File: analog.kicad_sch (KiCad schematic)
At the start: 51 parts, among them J10 Sensor harness, U9 ADS1115

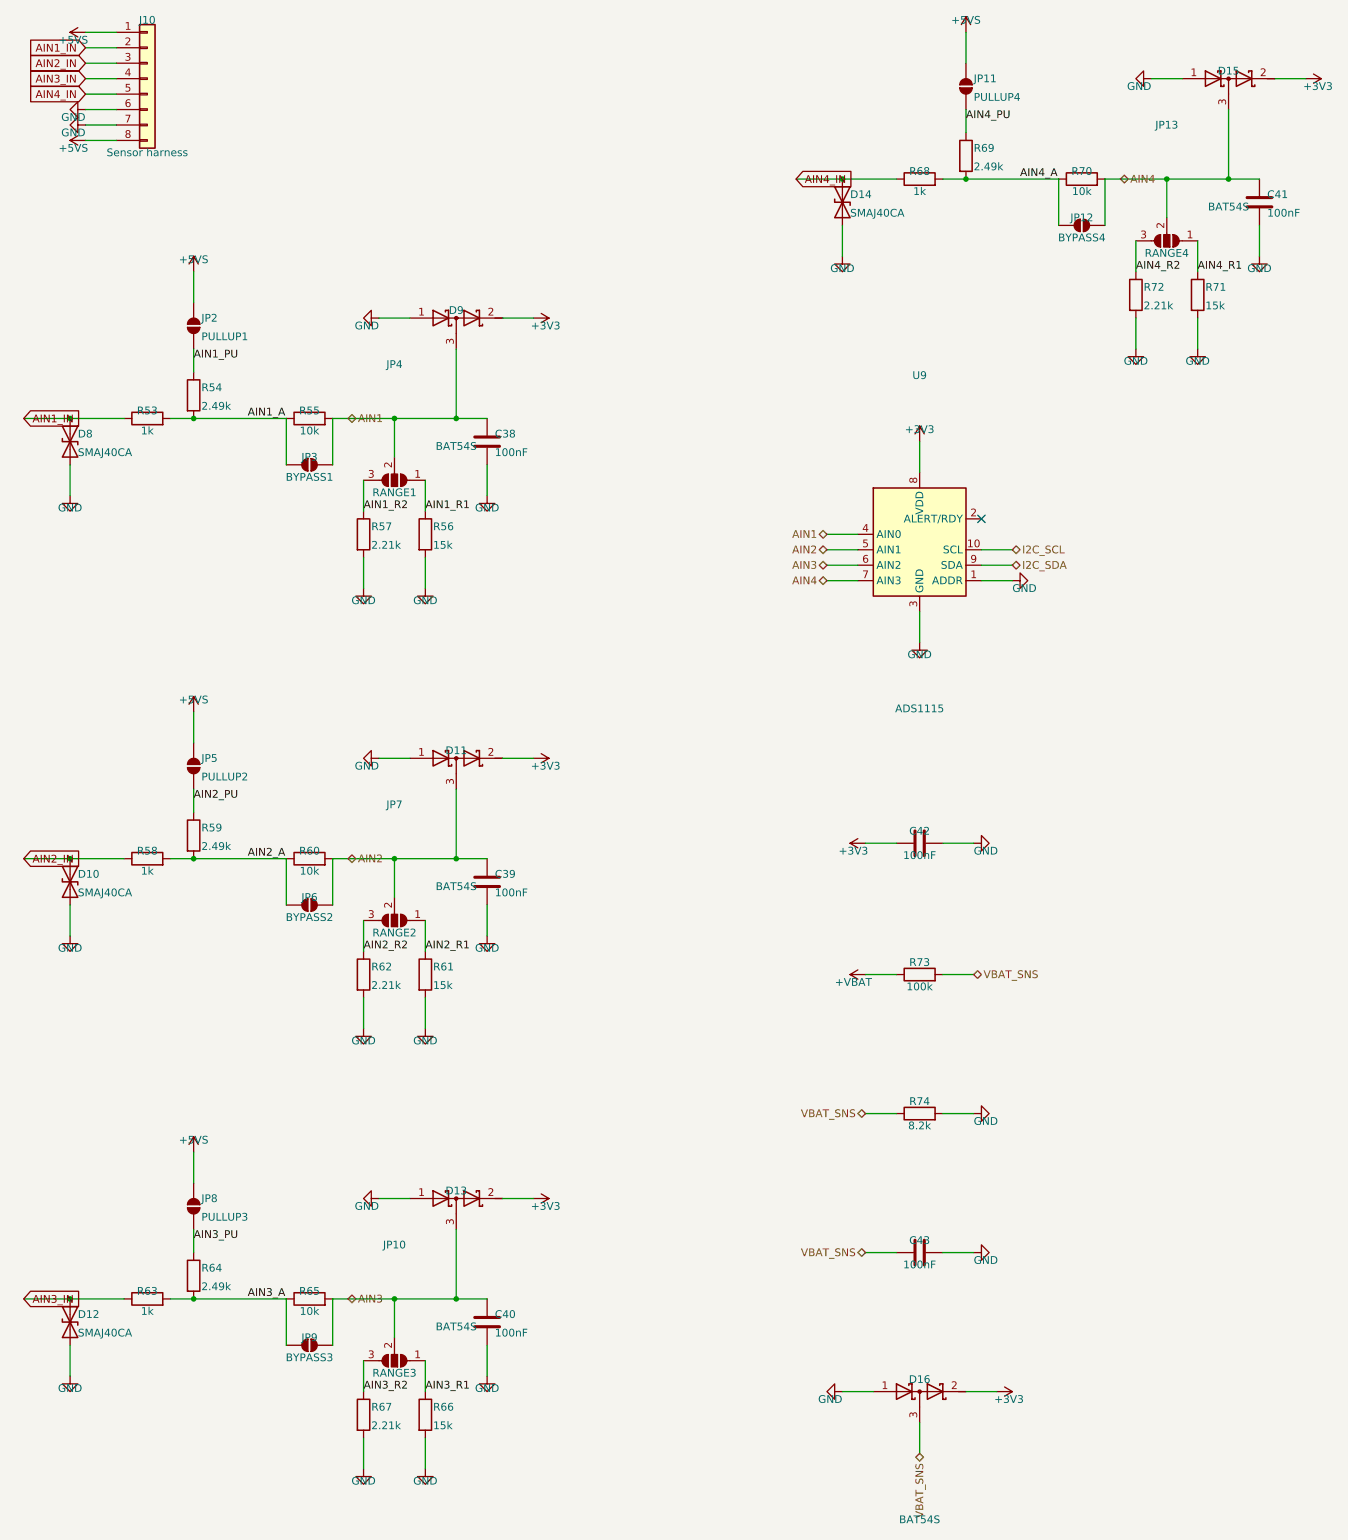
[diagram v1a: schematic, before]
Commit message: USB OVP, card-slot ESD, SD test points, and a gold-standard schematic
Hardware, all simulation- or review-driven:
- USB overvoltage cutoff: TLV431 + AO3401 + MMBT3906 series switch on
  VBUS, tripping at 5.77 V. Re-simulated: a compliant 5 V source passes
  at 4.99 V, the switch opens at 5.95 V of brick, and the +5V rail never
  exceeds 5.2 V from anything up to 14 V -- where a 9 V brick previously
  drove it to 8.4 V against the TJA1051's 6 V absolute maximum.
  Off-the-shelf OVP parts were rejected first: the TPS25200 class cuts
  off near 7 V, which is no protection for a 6 V limit.
- Two SRV05-4 arrays clamp every microSD card contact (LCSC C13612);
  until now the ESP32's ~2 kV pin diodes were all that stood behind a
  card swapped by hand after every session.
- A second USBLC6 clamps the USB-C CC pins -- the first contacts every
  plug insertion touches, previously landing on bare 5.1k resistors.
- Test points on SD_CLK and SD_CMD, the most likely scope targets at
  bring-up and otherwise reachable only on fine-pitch pads.

The schematic itself was rebuilt to read like a reference design
(RejsaCAN was the benchmark): every circuit is now a hand-drawn block --
power-fail detector, sensor-rail switch, USB OVP, connector pull-
resistor clusters, and a single utility panel for test points, ERC
flags, mounting holes and the power LED. Sentence-length values became
part numbers ("0.2A PTC", "AO3401A", "600R") with ratings kept in
hidden fields, which also answers the external review's value-hygiene
findings. Title blocks carry rev B and a date. The Power sheet shrank
from A2 back to A3 in the process.

gen/README.md now documents the whole pipeline -- stages, the block-
drawing conventions with per-rotation pin geometry, the junction rules,
and the traps (property newlines, off-grid points, anchors keeping
their natural rotation) -- so the next board reuses all of it.

Board: 84 x 100, 0 DRC violations, 0 unconnected, 0 courtyard overlaps,
physical audit clean. BOM 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
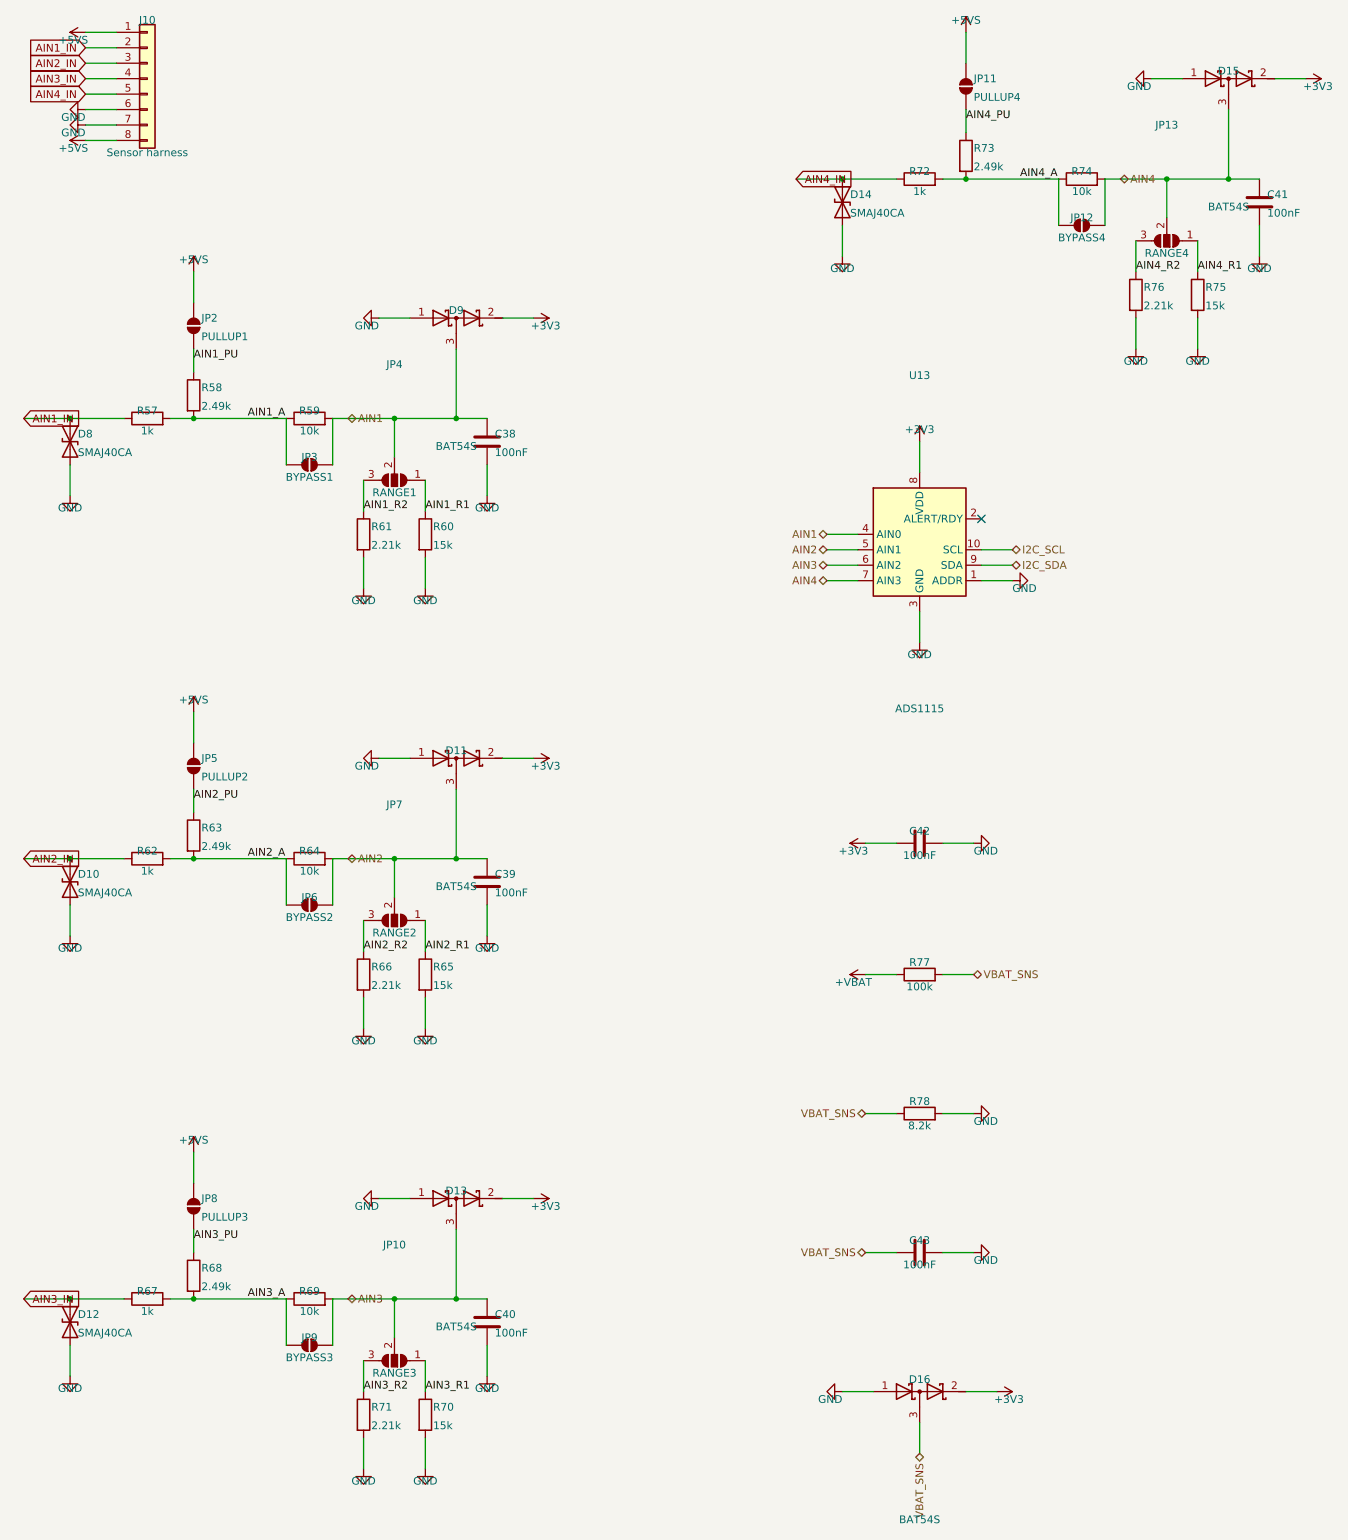
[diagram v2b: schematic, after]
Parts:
- removed R53: 1k, Resistor_SMD:R_0805_2012Metric, symbol Device:R
- removed R54: 2.49k, Resistor_SMD:R_0805_2012Metric, symbol Device:R
- removed R55: 10k, Resistor_SMD:R_0805_2012Metric, symbol Device:R
- removed R56: 15k, Resistor_SMD:R_0805_2012Metric, symbol Device:R
- removed U9: ADS1115, Package_SO:VSSOP-10_3x3mm_P0.5mm, symbol Analog_ADC:ADS1115IDGS
- added R75: 15k, Resistor_SMD:R_0805_2012Metric, symbol Device:R
- added R76: 2.21k, Resistor_SMD:R_0805_2012Metric, symbol Device:R
- added R77: 100k, Resistor_SMD:R_0805_2012Metric, symbol Device:R
- added R78: 8.2k, Resistor_SMD:R_0805_2012Metric, symbol Device:R
- added U13: ADS1115, Package_SO:VSSOP-10_3x3mm_P0.5mm, symbol Analog_ADC:ADS1115IDGS
- R57: value 2.21k -> 1k; Note 0-16V range: 16.0V in -> ~2.67V at the ADC (1k series inclu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 -> Ch1 series/fault-current limit; 0.1% thin film -- it is ins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
- R58: value 1k -> 2.49k; Note Ch2 series/fault-current limit; 0.1% thin film -- it is ins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 -> Ch1 bias resistor; Tolerance 0.1% -> (none)
- R59: value 2.49k -> 10k; Note Ch2 bias resistor -> Ch1 divider upper leg, 0.1% thin film for AFR-grade accuracy; Tolerance (none) -> 0.1%
- R60: value 10k -> 15k; Note Ch2 divider upper leg, 0.1% thin film for AFR-grade accuracy -> 0-5V range: 5.0V in -> ~2.88V at the ADC (1k series include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
- R61, R66, R71: value 15k -> 2.21k; Note 0-5V range: 5.0V in -> ~2.88V at the ADC (1k series include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 -> 0-16V range: 16.0V in -> ~2.67V at the ADC (1k series inclu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
- R62: value 2.21k -> 1k; Note 0-16V range: 16.0V in -> ~2.67V at the ADC (1k series inclu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 -> Ch2 series/fault-current limit; 0.1% thin film -- it is ins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
- R63: value 1k -> 2.49k; Note Ch3 series/fault-current limit; 0.1% thin film -- it is ins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 -> Ch2 bias resistor; Tolerance 0.1% -> (none)
- R64: value 2.49k -> 10k; Note Ch3 bias resistor -> Ch2 divider upper leg, 0.1% thin film for AFR-grade accuracy; Tolerance (none) -> 0.1%
- R65: value 10k -> 15k; Note Ch3 divider upper leg, 0.1% thin film for AFR-grade accuracy -> 0-5V range: 5.0V in -> ~2.88V at the ADC (1k series include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
- R67: value 2.21k -> 1k; Note 0-16V range: 16.0V in -> ~2.67V at the ADC (1k series inclu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 -> Ch3 series/fault-current limit; 0.1% thin film -- it is ins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
- R68: value 1k -> 2.49k; Note Ch4 series/fault-current limit; 0.1% thin film -- it is ins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 -> Ch3 bias resistor; Tolerance 0.1% -> (none)
- R69: value 2.49k -> 10k; Note Ch4 bias resistor -> Ch3 divider upper leg, 0.1% thin film for AFR-grade accuracy; Tolerance (none) -> 0.1%
- R70: value 10k -> 15k; Note Ch4 divider upper leg, 0.1% thin film for AFR-grade accuracy -> 0-5V range: 5.0V in -> ~2.88V at the ADC (1k series include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
- R72: value 2.21k -> 1k; Note 0-16V range: 16.0V in -> ~2.67V at the ADC (1k series inclu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 -> Ch4 series/fault-current limit; 0.1% thin film -- it is ins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
- R73: value 100k -> 2.49k; Note Battery monitor: divide by 11 -> Ch4 bias resistor
- R74: value 8.2k -> 10k; Note Divide by 13.2, not 11: at 36V the 11:1 divider put 3.27V o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 -> Ch4 divider upper leg, 0.1% thin film for AFR-grade accuracy; Tolerance (none) -> 0.1%
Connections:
- net +3V3: now also U13.8 (VDD)
- net +VBAT: now also R77.1; no longer R73.1
- net AIN1: now also R59.2, U13.4 (AIN0)
- net AIN1_A: now also R57.2, R58.2, R59.1
- net AIN1_IN: now also R57.1
- net AIN1_PU: now also R58.1
- net AIN1_R1: now also R60.1
- net AIN1_R2: now also R61.1; no longer R57.1
- net AIN2: now also R64.2, U13.5 (AIN1); no longer R60.2
- net AIN2_A: now also R62.2, R63.2, R64.1; no longer R58.2, R59.2, R60.1
- net AIN2_IN: now also R62.1; no longer R58.1
- net AIN2_PU: now also R63.1; no longer R59.1
- net AIN2_R1: now also R65.1; no longer R61.1
- net AIN2_R2: now also R66.1; no longer R62.1
- net AIN3: now also R69.2, U13.6 (AIN2); no longer R65.2
- net AIN3_A: now also R67.2, R68.2, R69.1; no longer R63.2, R64.2, R65.1
- net AIN3_IN: now also R67.1; no longer R63.1
- net AIN3_PU: now also R68.1; no longer R64.1
- net AIN3_R1: now also R70.1; no longer R66.1
- net AIN3_R2: now also R71.1; no longer R67.1
- net AIN4: now also R74.2, U13.7 (AIN3); no longer R70.2
- net AIN4_A: now also R72.2, R73.2, R74.1; no longer R68.2, R69.2, R70.1
- net AIN4_IN: now also R72.1; no longer R68.1
- net AIN4_PU: now also R73.1; no longer R69.1
- net AIN4_R1: now also R75.1; no longer R71.1
- net AIN4_R2: now also R76.1; no longer R72.1
- net GND: now also R60.2, R65.2, R70.2, R75.2, R76.2, R78.2, U13.1 (ADDR), U13.3 (GND); no longer R57.2, R62.2, R67.2, R72.2, R74.2
- net I2C_SCL: now also U13.10 (SCL)
- net I2C_SDA: now also U13.9 (SDA)
- net VBAT_SNS: now also R77.2, R78.1; no longer R73.2, R74.1
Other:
- moved on the sheet: R57, R58, R59, R60, R61, R62, R63, R64, R65, R66, R67, R68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

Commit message: Studies 9-11, post-route extraction, strap audit, readable labels, production BOM numbers
New tests, run against the final board:
- audit_routes.py: Dijkstra IR drop over the routed copper (worst 55 mV
  at rated current), SD/USB/CAN routed lengths (USB pair matched to
  1.1 mm), buck switch-node copper area. All clean.
- audit_straps.py: every ESP32-S3 strapping pin against what the netlist
  hangs on it; all five boot in their required state.
- simulate.py 9, stability: the LM5164 ripple-injection criterion across
  the input window. Found the ramp thin (10.6 mV) at a legitimate 8 V
  operating point -- ramp caps changed 3.3 nF -> 2.2 nF, now 15.8 mV+
  everywhere above crank voltages. Board rebuilt: 0 DRC, 0 unconnected,
  0 overlaps.
- simulate.py 10, CAN bus: TJA1051 through the choke and split
  termination into 5 m of terminated line -- 2.00 V dominant at the far
  end, no overshoot.
- simulate.py 11, budgets: enclosure thermal for the in-dash mount
  (sealed ABS is fine in the dash, would exceed the electrolytics' 105 C
  in an engine bay -- documented), fuse derating 69 %, I2C rise time vs
  Qwiic chains, WS2812 count, SD switch drop, connector contacts.
- tolerance MC gains the ride-through corner: 36 ms at caps -20 % /
  load +40 %, still covering a healthy-card flush.

Schematic readability, second pass: net-name labels moved onto short
vertical spurs clear of the circuits (deleting them outright renames
nets to Net-(R5-Pad2) and breaks name-based verification -- now in
gen/README.md), end-labels extend away from what they feed, and the
sensor-switch block redrawn at 1.5x pitch. Reversed-5V behaviour per
connector documented in the README.

BOM production pass: verified LCSC numbers added for the TVS families,
BAT54S, MM3Z zener and 2N7002s (21 numbered lines); the 39 blank lines
are JLC-auto-matched basic R/C; the 12 extended lines that must be
hand-matched in the order UI are listed in README 11. No guessed part
numbers.

gen/README.md gains the readab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
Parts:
- D11, D13, D15, D16, D9: MPN BAT54S -> MDD BAT54S
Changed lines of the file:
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@@
       (effects (font (size 1.27 1.27)) hide)
     )
-    (property "MPN" "BAT54S" (at 97.79 85.85 0)
+    (property "MPN" "MDD BAT54S" (at 97.79 85.85 0)
       (effects (font (size 1.27 1.27)) hide)
     )
@@
       (effects (font (size 1.27 1.27)) hide)
     )
-    (property "MPN" "BAT54S" (at 97.79 158.24 0)
+    (property "MPN" "MDD BAT54S" (at 97.79 158.24 0)
       (effects (font (size 1.27 1.27)) hide)
     )
@@
       (effects (font (size 1.27 1.27)) hide)
     )
-    (property "MPN" "BAT54S" (at 97.79 230.63 0)
+    (property "MPN" "MDD BAT54S" (at 97.79 230.63 0)
       (effects (font (size 1.27 1.27)) hide)
     )
@@
       (effects (font (size 1.27 1.27)) hide)
     )
-    (property "MPN" "BAT54S" (at 224.79 46.48 0)
+    (property "MPN" "MDD BAT54S" (at 224.79 46.48 0)
       (effects (font (size 1.27 1.27)) hide)
     )
@@
       (effects (font (size 1.27 1.27)) hide)
     )
-    (property "MPN" "BAT54S" (at 173.99 262.35 0)
-      (effects (font (size 1.27 1.27)) hide)
-    )
+    (property "MPN" "MDD BAT54S" (at 173.99 262.35 0)
+      (effects (font (size 1.27 1.27)) hide)
+    )
